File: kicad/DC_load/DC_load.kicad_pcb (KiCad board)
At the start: 2 copper layers, 110 x 145 mm, 147 parts, among them J1 Conn_Coaxial, J2 red_terminal, J3 red terminal, J4 black terminal, J5 black terminal, J6 USB_B, J7 Conn_01x06_Socket, J9 Conn_01x04_Socket, Q1 MMBT5401, Q3 FQP19N20C, Q4 FQP19N20C, Q5 FQP19N20C, Q6 FQP19N20C, SW1 RotaryEncoder_Switch, SW2 RotaryEncoder_Switch, SW3 SW_Push, SW8 SW_Push, U1 FSA3157P6X, U10 FSA3157P6X, U11 FSA3157P6X, U12 FSA3157P6X, U13 TLV9062, U14 AMS1117-3.3, U15 74HC14D653, U16 LM4040DBZ-3, U17 CH340C, U2 Screen, U3 NCS21802, U4 NCS21802, U5 TLV9062, U6 TLV9062, U7 LMT84LPM, U8 STM32F103C8Tx

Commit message: Oa.
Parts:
- removed J7: Conn_01x06_Socket, Connector_PinSocket_2.54mm:PinSocket_1x06_P2.54mm_Vertical
- removed U16: LM4040DBZ-3, Package_TO_SOT_SMD:SOT-23
- added C48: 100n, Capacitor_SMD:C_0603_1608Metric_Pad1.08x0.95mm_HandSolder, F.Cu at (52.8, 174.9)
- added C49: 100n, Capacitor_SMD:C_0603_1608Metric_Pad1.08x0.95mm_HandSolder, F.Cu at (104.6, 190.6)
- added C50: 100n, Capacitor_SMD:C_0603_1608Metric_Pad1.08x0.95mm_HandSolder, F.Cu at (103.6, 176.0)
- added C51: 100n, Capacitor_SMD:C_0603_1608Metric_Pad1.08x0.95mm_HandSolder, F.Cu at (108.0, 182.3)
- added C52: 100n, Capacitor_SMD:C_0603_1608Metric_Pad1.08x0.95mm_HandSolder, F.Cu at (107.2, 189.6)
- added J8: Conn_01x05_Socket, Connector_PinSocket_2.54mm:PinSocket_1x05_P2.54mm_Vertical, B.Cu at (118.8, 180.8)
- added R56: 10k, Resistor_SMD:R_0603_1608Metric_Pad0.98x0.95mm_HandSolder, F.Cu at (98.9, 191.3)
- added R57: 49.9k, Resistor_SMD:R_0603_1608Metric_Pad0.98x0.95mm_HandSolder, F.Cu at (101.6, 193.8)
- added R58: 10k, Resistor_SMD:R_0603_1608Metric_Pad0.98x0.95mm_HandSolder, F.Cu at (97.0, 183.6)
- added U18: TL431DBZ, Package_TO_SOT_SMD:SOT-23, F.Cu at (101.6, 191.3)
- C33: value 100n -> 10u
- J1: value Conn_Coaxial -> BNC
- J6: footprint Connector_USB:USB_B_OST_USB-B1HSxx_Horizontal -> DC_load:62910416121
- JP1, JP2: moved to B.Cu
- R30, R33: value 50k -> 49.9k
- SW1, SW2: footprint DC_load:rotary_encoder_bottom_solder -> Rotary_Encoder:RotaryEncoder_Alps_EC11E-Switch_Vertical_H20mm
- U9: value ~ -> Front plate
- moved R50 201.3 mm to (54.6, 176.0), turned to 90 degrees
- moved R52 198.1 mm to (56.2, 176.0), turned to -90 degrees
- moved R51 197.5 mm to (61.3, 184.7), turned to 180 degrees
- moved C44 188.8 mm to (59.9, 174.5), turned to 180 degrees
- moved C45 187.4 mm to (64.8, 184.7), turned to 180 degrees
- moved C47 182.6 mm to (60.3, 180.4), turned to -90 degrees
- moved R53 181.6 mm to (61.3, 183.0)
- moved D4 175.2 mm to (94.0, 190.6), turned to -90 degrees
- moved D3 174.5 mm to (94.0, 185.9), turned to -90 degrees
- moved R35 172.2 mm to (95.9, 191.3), turned to -90 degrees
- moved C35 169.0 mm to (97.0, 185.2)
- moved Q1 157.1 mm to (97.3, 187.8)
- moved R34 149.6 mm to (97.4, 191.3), turned to 90 degrees
- moved C34 145.9 mm to (100.4, 186.6), turned to -45 degrees
- moved C33 141.9 mm to (96.8, 193.7)
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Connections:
- C33 pad 1: GND -> +5V
- C33 pad 2: VREF -> GND
- J9 pad 2: +3V3 -> 3V3
- R34 pad 1: VREF -> +5V
- R34 pad 2: +5V -> VREF
- R36 pad 1: +3V3 -> 3V3
- R37 pad 1: +3V3 -> 3V3
- R39 pad 1: +3V3 -> 3V3
- R41 pad 1: +3V3 -> 3V3
- R43 pad 1: +3V3 -> 3V3
- R45 pad 1: +3V3 -> 3V3
- R51 pad 1: +3V3 -> 3V3
- R54 pad 1: +3V3 -> 3V3
- R55 pad 1: +3V3 -> 3V3
- SW3 pad 2: +3V3 -> 3V3
- U13 pad 5: unconnected-(U13B-+-Pad5) -> GND
- U13 pad 6: unconnected-(U13B---Pad6) -> Net-(U13B--)
- U13 pad 7: unconnected-(U13-Pad7) -> Net-(U13B--)
- U8 pad 15: unconnected-(U8-PA5-Pad15) -> CTRL_SEL
- U8 pad 16: CH3_PWM -> CH1_PWM
- U8 pad 17: CH4_PWM -> CH2_PWM
- U8 pad 2: unconnected-(U8-PC13-Pad2) -> ENC_A_1
- U8 pad 20: unconnected-(U8-PB2-Pad20) -> ENC_SW_2
- U8 pad 27: unconnected-(U8-PB14-Pad27) -> ENC_A_2
- U8 pad 28: unconnected-(U8-PB15-Pad28) -> ENC_B_2
- U8 pad 29: CH1_PWM -> CH3_PWM
- U8 pad 3: unconnected-(U8-PC14-Pad3) -> ENC_SW_1
- U8 pad 38: CH2_PWM -> CH4_PWM
- U8 pad 4: unconnected-(U8-PC15-Pad4) -> ENC_B_1
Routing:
- net /Microcontroller/CH4_MEAS: track 0.00 -> 141.1 mm, vias 0 -> 1
- net /Microcontroller/CH2_MEAS: track 0.00 -> 136.9 mm, vias 0 -> 1
- net /Microcontroller/CH3_MEAS: track 0.00 -> 122.0 mm, vias 0 -> 1
- net /Microcontroller/CH1_MEAS: track 0.00 -> 117.2 mm, vias 0 -> 1
- net +5V: track 0.00 -> 93.8 mm, vias 0 -> 2
- net BOOT: track 0.00 -> 66.1 mm, vias 0 -> 1
- net /Microcontroller/TX2: track 0.00 -> 46.4 mm
- net ENC_SW_1: track 0.00 -> 38.4 mm, vias 0 -> 1
- net CH1_PWM: track 0.00 -> 24.1 mm, vias 0 -> 1
- net GND: track 0.00 -> 17.0 mm, vias 0 -> 5
- net ENC_B_1: track 0.00 -> 16.9 mm, vias 0 -> 1
- net ENC_A_1: track 0.00 -> 16.3 mm, vias 0 -> 1
- net RX: track 0.00 -> 14.9 mm, vias 0 -> 2
- net TX: track 0.00 -> 12.2 mm, vias 0 -> 1
- net VREF: track 0.00 -> 12.1 mm, vias 0 -> 1
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- added copper zone on F.Cu, net 3V3

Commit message: Compressed.
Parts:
- C12, C13, C14, C15, R14, R15, R3, R9: moved to B.Cu
- moved C15 12.4 mm to (126.8, 120.7), turned to -45 degrees
- moved R12 11.0 mm to (120.3, 114.1)
- moved R14 9.55 mm to (130.4, 117.3)
- moved C14 9.27 mm to (83.4, 120.8), turned to -135 degrees
- moved R15 8.02 mm to (123.3, 73.6)
- moved C1 7.98 mm to (93.6, 109.0)
- moved C10 7.98 mm to (104.8, 103.4)
- moved C11 7.98 mm to (104.6, 109.0)
- moved C16 7.98 mm to (116.0, 113.0)
- moved C17 7.98 mm to (96.0, 115.5)
- moved C18 7.98 mm to (95.0, 83.3)
- moved C19 7.98 mm to (118.5, 82.5)
- moved C2 7.98 mm to (98.8, 89.0)
- moved C21 7.98 mm to (92.0, 116.8)
- moved C22 7.98 mm to (92.0, 113.8)
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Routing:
- net /Microcontroller/CH1_MEAS: track 117.2 -> 39.1 mm
- net /Microcontroller/CH2_MEAS: track 136.9 -> 215.1 mm
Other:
- board text added: "NO THERMAL PADS; VIN needs no polygon"

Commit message: Most routing done.
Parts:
- moved C10 18.2 mm to (105.0, 85.2)
- moved D2 15.2 mm to (154.2, 133.1), turned to 90 degrees
- moved C9 14.4 mm to (104.9, 104.4)
- moved D1 13.3 mm to (156.7, 133.1), turned to -90 degrees
- moved J8 11.2 mm to (109.7, 174.2), turned to -90 degrees
- moved R20 8.50 mm to (152.1, 132.3), turned to 90 degrees
- moved C17 3.30 mm to (98.6, 113.5), turned to -90 degrees
- moved R54 2.55 mm to (110.9, 190.4), turned to 0 degrees
- moved R6 2.51 mm to (98.8, 90.1)
- moved U6 2.48 mm to (105.0, 88.7)
- moved R41 2.33 mm to (140.6, 184.9)
- moved C2 1.85 mm to (97.3, 90.1)
- moved R8 1.85 mm to (95.5, 90.1)
- moved U1 1.71 mm to (95.3, 114.7)
- moved C38 1.20 mm to (141.2, 182.4), turned to 90 degrees
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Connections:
- net /Microcontroller/TX2 renamed Net-(U8-PA2)
- C31 pad 1: +5V -> 5V
- C33 pad 1: +5V -> 5V
- C8 pad 1: +5V -> 5V
- D4 pad 2: +5V -> 5V
- J6 pad 1: +5V -> 5V
- J8 pad 1: RX -> /Microcontroller/PROG_RX
- J8 pad 2: TX -> /Microcontroller/PROG_TX
- R34 pad 1: +5V -> 5V
- R35 pad 2: +5V -> 5V
- U14 pad 3: +5V -> 5V
- U7 pad 1: +5V -> 5V
- U8 pad 20: ENC_SW_2 -> unconnected-(U8-PB2-Pad20)
- U8 pad 27: ENC_A_2 -> unconnected-(U8-PB14-Pad27)
- U8 pad 28: ENC_B_2 -> unconnected-(U8-PB15-Pad28)
- U8 pad 30: RX -> /Microcontroller/PROG_RX
- U8 pad 31: TX -> /Microcontroller/PROG_TX
- U8 pad 39: unconnected-(U8-PB3-Pad39) -> ENC_B_2
- U8 pad 40: unconnected-(U8-PB4-Pad40) -> ENC_A_2
- U8 pad 41: unconnected-(U8-PB5-Pad41) -> ENC_SW_2
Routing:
- net Net-(R23-Pad2): track 0.00 -> 196.3 mm, vias 0 -> 2
- net /Power_stage/V_SENSE-: track 0.00 -> 184.0 mm
- net Net-(R22-Pad2): track 0.00 -> 170.3 mm, vias 0 -> 2
- net 5V: track 0.00 -> 150.9 mm, vias 0 -> 2
- net CTRL_SEL: track 1.72 -> 117.7 mm, vias 1 -> 3
- net /Power_stage/V_SENSE+: track 0.00 -> 111.4 mm
- net Net-(R27-Pad2): track 0.00 -> 106.2 mm, vias 0 -> 2
- net Net-(R25-Pad2): track 0.00 -> 103.1 mm, vias 0 -> 2
- net +5V: track 93.8 -> 0.00 mm, vias 2 -> 0
- net /Microcontroller/CH1_MEAS: track 39.1 -> 118.8 mm, vias 1 -> 3
- net /Microcontroller/CH2_MEAS: track 215.1 -> 138.8 mm, vias 1 -> 3
- net 3V3: track 6.14 -> 71.9 mm, vias 4 -> 7
- net CH2_PWM: track 2.58 -> 62.5 mm
- net /Microcontroller/BNC_CONTROL: track 0.00 -> 58.7 mm, vias 0 -> 2
- net CH3_PWM: track 0.00 -> 57.1 mm, vias 0 -> 1
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- added copper zone on F.Cu, net 5V

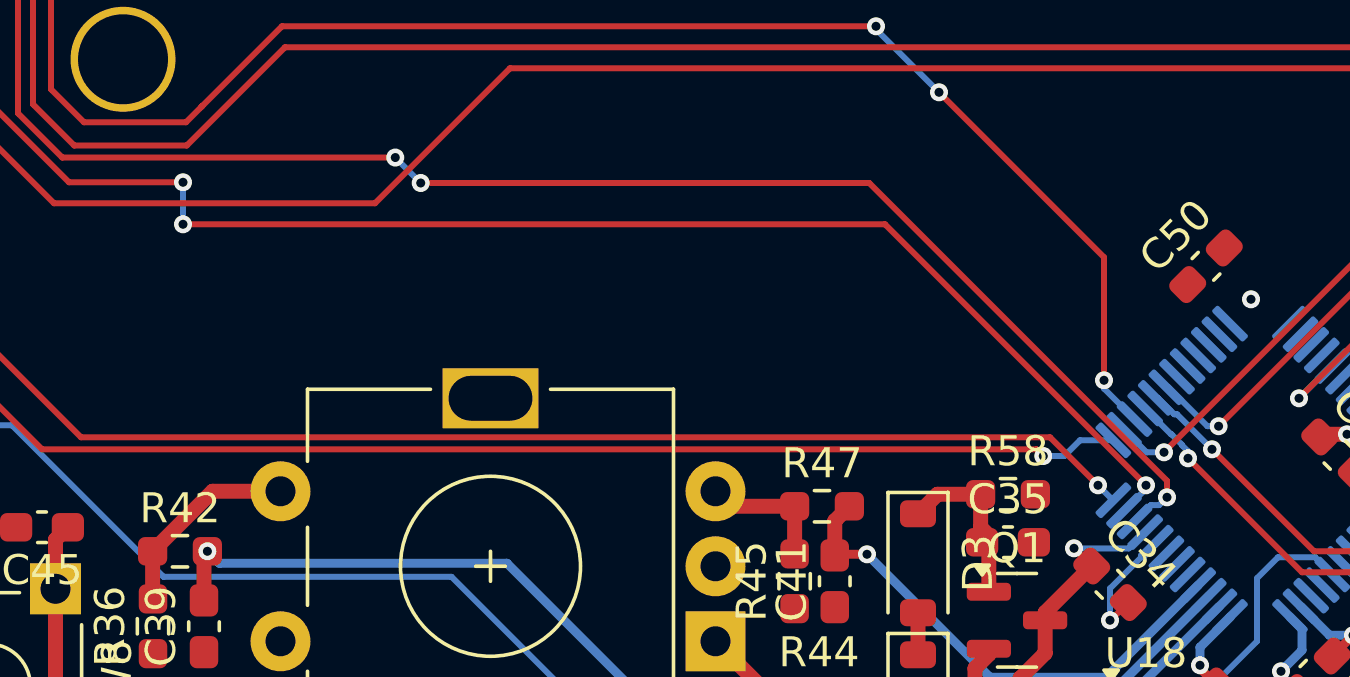
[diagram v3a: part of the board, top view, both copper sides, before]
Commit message: Added EEPROM
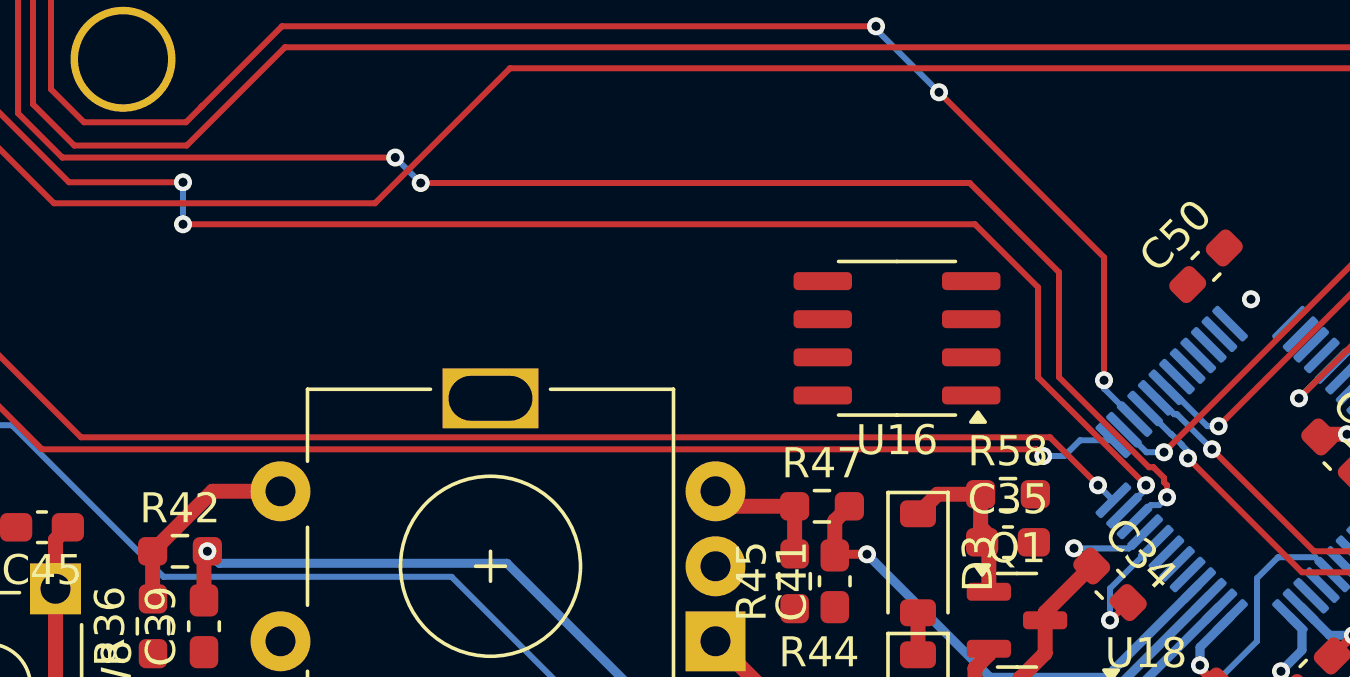
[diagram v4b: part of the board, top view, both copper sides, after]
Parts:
- added U16: 93LCxxB, Package_SO:SOIC-8_3.9x4.9mm_P1.27mm, F.Cu at (93.3, 178.4)
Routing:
- net /Microcontroller/CH1_MEAS: track 118.8 -> 120.8 mm
- net /Microcontroller/CH2_MEAS: track 138.8 -> 140.5 mm

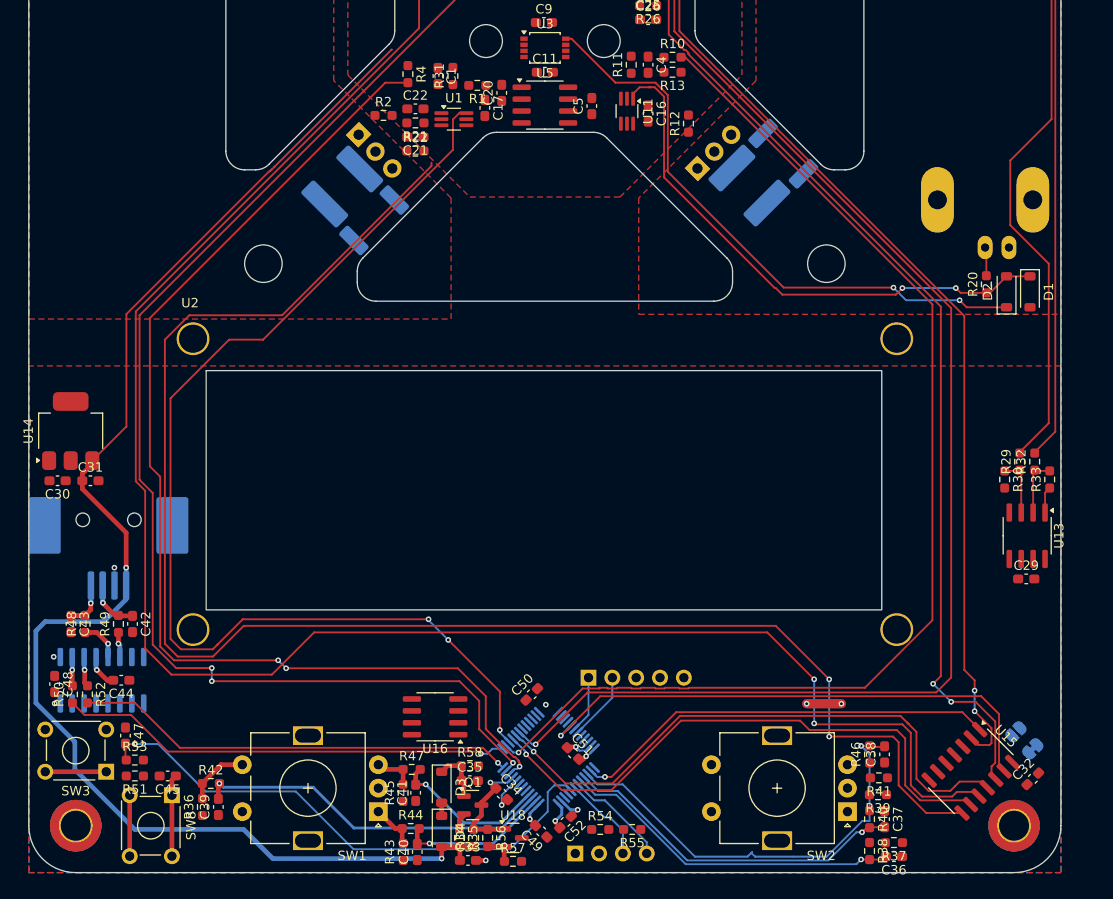
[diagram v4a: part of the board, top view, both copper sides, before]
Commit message: MCU almost routed.
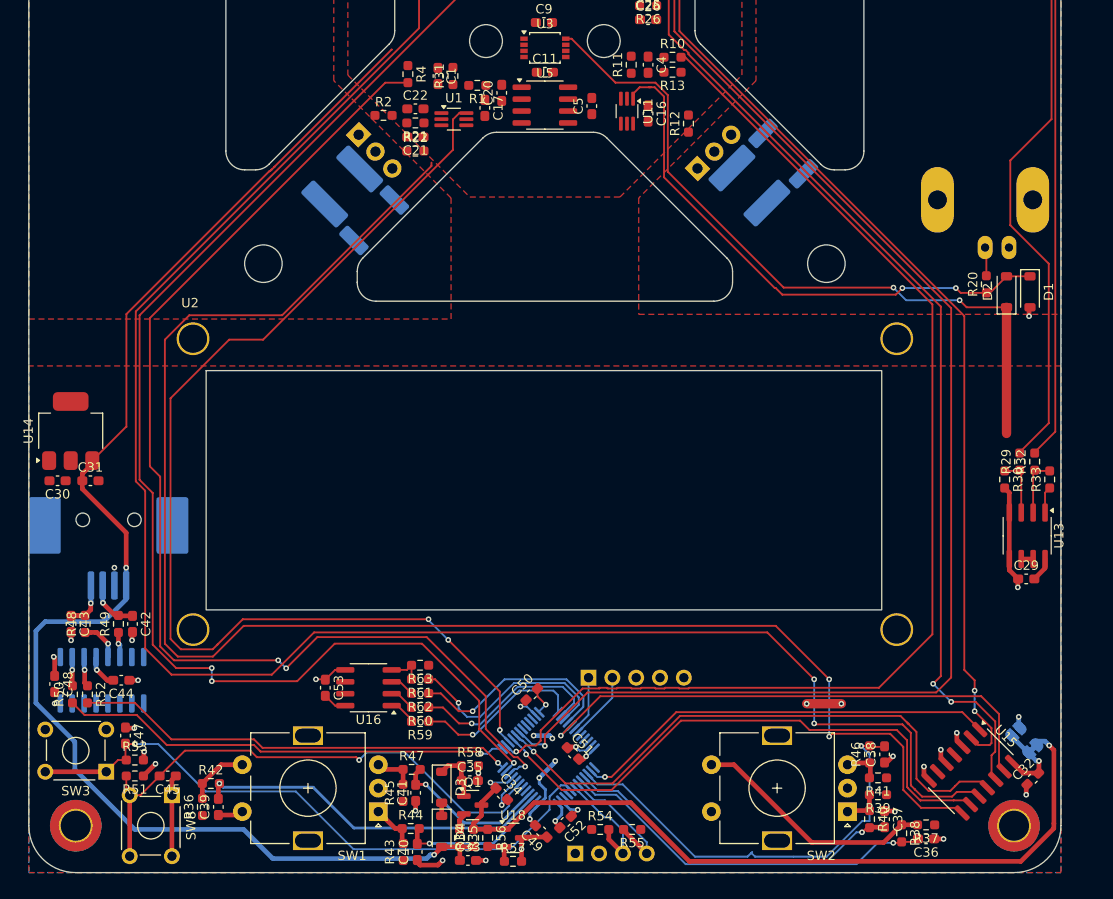
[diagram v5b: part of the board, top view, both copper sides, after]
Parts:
- added C53: 100n, Capacitor_SMD:C_0603_1608Metric_Pad1.08x0.95mm_HandSolder, F.Cu at (81.6, 175.3)
- added R59: 100, Resistor_SMD:R_0603_1608Metric_Pad0.98x0.95mm_HandSolder, F.Cu at (91.7, 178.9)
- added R60: 100, Resistor_SMD:R_0603_1608Metric_Pad0.98x0.95mm_HandSolder, F.Cu at (91.7, 177.4)
- added R61: 100, Resistor_SMD:R_0603_1608Metric_Pad0.98x0.95mm_HandSolder, F.Cu at (91.7, 174.4)
- added R62: 100, Resistor_SMD:R_0603_1608Metric_Pad0.98x0.95mm_HandSolder, F.Cu at (91.7, 175.9)
- added R63: 10k, Resistor_SMD:R_0603_1608Metric_Pad0.98x0.95mm_HandSolder, F.Cu at (91.7, 172.9)
- moved U16 7.75 mm to (86.2, 175.3)
- moved C36 3.91 mm to (145.6, 191.4)
- moved R37 3.91 mm to (145.6, 189.9)
- moved R38 3.91 mm to (143.0, 190.8)
- moved R41 0.10 mm to (140.5, 184.9)
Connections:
- U16 pad 1: unconnected-(U16-CS-Pad1) -> Net-(U16-CS)
- U16 pad 2: unconnected-(U16-SCLK-Pad2) -> Net-(U16-SCLK)
- U16 pad 3: unconnected-(U16-DI-Pad3) -> Net-(U16-DI)
- U16 pad 4: unconnected-(U16-DO-Pad4) -> Net-(U16-DO)
- U16 pad 5: unconnected-(U16-GND-Pad5) -> GND
- U16 pad 8: unconnected-(U16-VCC-Pad8) -> 3V3
- U8 pad 25: unconnected-(U8-PB12-Pad25) -> Net-(U8-PB12)
- U8 pad 26: unconnected-(U8-PB13-Pad26) -> Net-(U8-PB13)
- U8 pad 27: unconnected-(U8-PB14-Pad27) -> Net-(U8-PB14)
- U8 pad 28: unconnected-(U8-PB15-Pad28) -> Net-(U8-PB15)
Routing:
- net VREF: track 12.1 -> 86.5 mm, vias 1 -> 2
- net RESET: track 6.50 -> 57.6 mm, vias 0 -> 1
- net GND: track 23.6 -> 70.4 mm, vias 8 -> 28
- net 3V3: track 71.9 -> 104.3 mm, vias 7 -> 13
- net Net-(R37-Pad2): track 0.00 -> 26.2 mm
- net Net-(U8-PB14): track 0.00 -> 23.0 mm, vias 0 -> 1
- net Net-(U8-PB15): track 0.00 -> 22.9 mm, vias 0 -> 1
- net Net-(U8-PB13): track 0.00 -> 20.8 mm, vias 0 -> 1
- net Net-(U8-PB12): track 0.00 -> 18.3 mm, vias 0 -> 1
- net Net-(JP1-A): track 0.00 -> 8.13 mm, vias 0 -> 1
- net ENC_SW_2: track 36.5 -> 40.7 mm
- net Net-(R39-Pad2): track 0.00 -> 4.09 mm
- net Net-(R41-Pad2): track 0.00 -> 4.05 mm
- net Net-(U16-DO): track 0.00 -> 3.82 mm
- net /Microcontroller/CH1_MEAS: track 120.8 -> 124.5 mm
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
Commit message: MIddle.
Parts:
- moved R16 5.70 mm to (115.5, 94.8)
- moved R4 2.41 mm to (92.0, 108.1), turned to 90 degrees
- moved C7 1.90 mm to (115.5, 91.4), turned to -90 degrees
- moved R18 1.90 mm to (113.8, 91.4), turned to 90 degrees
- moved U4 1.80 mm to (105.0, 95.3)
- moved C46 1.68 mm to (104.9, 92.7)
- moved R1 1.41 mm to (96.8, 110.1), turned to -90 degrees
- moved C6 0.50 mm to (109.6, 87.8)
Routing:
- net /Microcontroller/CH1_MEAS: track 124.5 -> 146.4 mm
- net Net-(C20-Pad2): track 0.00 -> 15.8 mm
- net /Microcontroller/CH2_MEAS: track 144.0 -> 158.6 mm
- net Net-(C3-Pad2): track 0.00 -> 14.3 mm
- net Net-(U4B--): track 0.00 -> 13.2 mm
- net /Microcontroller/CH4_MEAS: track 147.7 -> 158.7 mm
- net Net-(U4A--): track 0.00 -> 9.56 mm
- net CH1_CONTROL: track 0.00 -> 6.52 mm
- net Net-(U6A--): track 0.00 -> 4.67 mm
- net Net-(U6B--): track 0.00 -> 4.23 mm
- net Net-(C23-Pad2): track 0.00 -> 3.92 mm
- net Net-(C22-Pad2): track 0.00 -> 3.48 mm
- net Net-(C1-Pad1): track 0.00 -> 3.31 mm
- net Net-(C24-Pad2): track 0.00 -> 3.25 mm
- net Net-(U3A--): track 0.00 -> 3.22 mm
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
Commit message: kldsjfald.
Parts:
- moved R4 12.8 mm to (103.8, 103.1), turned to 0 degrees
- moved C1 11.0 mm to (100.4, 101.5), turned to 180 degrees
- moved R31 8.72 mm to (100.4, 103.1), turned to 0 degrees
- moved R1 7.83 mm to (97.9, 102.3)
- moved U12 3.43 mm to (116.8, 86.7), turned to 90 degrees
- moved R17 3.33 mm to (122.7, 84.8), turned to 135 degrees
- moved C9 2.77 mm to (107.3, 103.1)
- moved C11 2.32 mm to (106.8, 108.3)
- moved C19 2.04 mm to (116.8, 82.5)
- moved C20 1.40 mm to (100.4, 110.5)
- moved U5 1.40 mm to (105.0, 111.8)
- moved C5 1.40 mm to (110.0, 111.9)
- moved U3 1.40 mm to (105.0, 105.7)
- moved R7 0.92 mm to (91.3, 79.5)
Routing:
- net Net-(Q3-S): track 0.00 -> 34.2 mm, vias 0 -> 2
- net Net-(C6-Pad2): track 2.59 -> 19.4 mm
- net CH2_CONTROL: track 0.00 -> 7.07 mm, vias 0 -> 2
- net Net-(U3A--): track 3.22 -> 7.51 mm
- net /Microcontroller/CH1_MEAS: track 146.4 -> 150.5 mm
- net /Microcontroller/CH2_MEAS: track 158.6 -> 162.5 mm
- net Net-(C28-Pad2): track 0.00 -> 3.59 mm
- net Net-(C27-Pad2): track 0.00 -> 3.00 mm
- net Net-(Q4-G): track 0.00 -> 2.49 mm
- net Net-(Q6-G): track 0.00 -> 2.25 mm
- net Net-(C1-Pad1): track 3.31 -> 4.80 mm
- net CH1_CONTROL: track 6.52 -> 7.72 mm
- net Net-(C3-Pad2): track 14.3 -> 13.5 mm

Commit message: sdaf
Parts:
- moved C25 3.00 mm to (116.0, 98.1)
- moved C26 1.50 mm to (116.0, 102.6)
- moved R26 1.50 mm to (116.0, 101.1)
- moved R17 0.66 mm to (122.0, 84.9), turned to 180 degrees
- moved R8 0.20 mm to (95.7, 90.1)
- moved C27 0.15 mm to (120.1, 89.8)
- moved C28 0.15 mm to (120.1, 86.8)
- moved R27 0.15 mm to (120.1, 91.3)
- moved R28 0.15 mm to (120.1, 88.3)
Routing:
- net GND: track 70.5 -> 113.4 mm, vias 28 -> 58
- net Net-(Q6-S): track 0.00 -> 30.8 mm, vias 0 -> 2
- net Net-(Q4-S): track 0.00 -> 26.2 mm, vias 0 -> 2
- net Net-(Q5-S): track 0.00 -> 25.3 mm, vias 0 -> 1
- net Net-(C26-Pad2): track 0.00 -> 13.9 mm, vias 0 -> 2
- net Net-(C4-Pad1): track 0.00 -> 13.8 mm
- net CH4_CONTROL: track 0.00 -> 12.6 mm
- net Net-(U3B--): track 0.00 -> 12.0 mm
- net Net-(Q3-S): track 34.2 -> 26.5 mm
- net CH3_CONTROL: track 0.00 -> 6.46 mm, vias 0 -> 2
- net 5V: track 150.2 -> 154.9 mm, vias 2 -> 3
- net Net-(Q5-G): track 0.00 -> 4.26 mm
- net Net-(C25-Pad2): track 0.00 -> 3.02 mm
- net CTRL_SEL: track 117.7 -> 119.7 mm, vias 3 -> 5
- net 3V3: track 106.6 -> 104.7 mm, vias 13 -> 14
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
